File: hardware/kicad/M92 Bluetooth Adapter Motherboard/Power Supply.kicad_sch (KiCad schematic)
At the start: 35 parts, among them IC11 MCP1702T-5002E_CB, IC12 TPS22810DBVR, IC13 TPS22917DBVR, IC4 NJU7031D, IC4 TL7660IDR, J1 Conn_External_Power, J4 B2B-XH-A, J5 B2B-XH-A, J9 B6B-XH-A

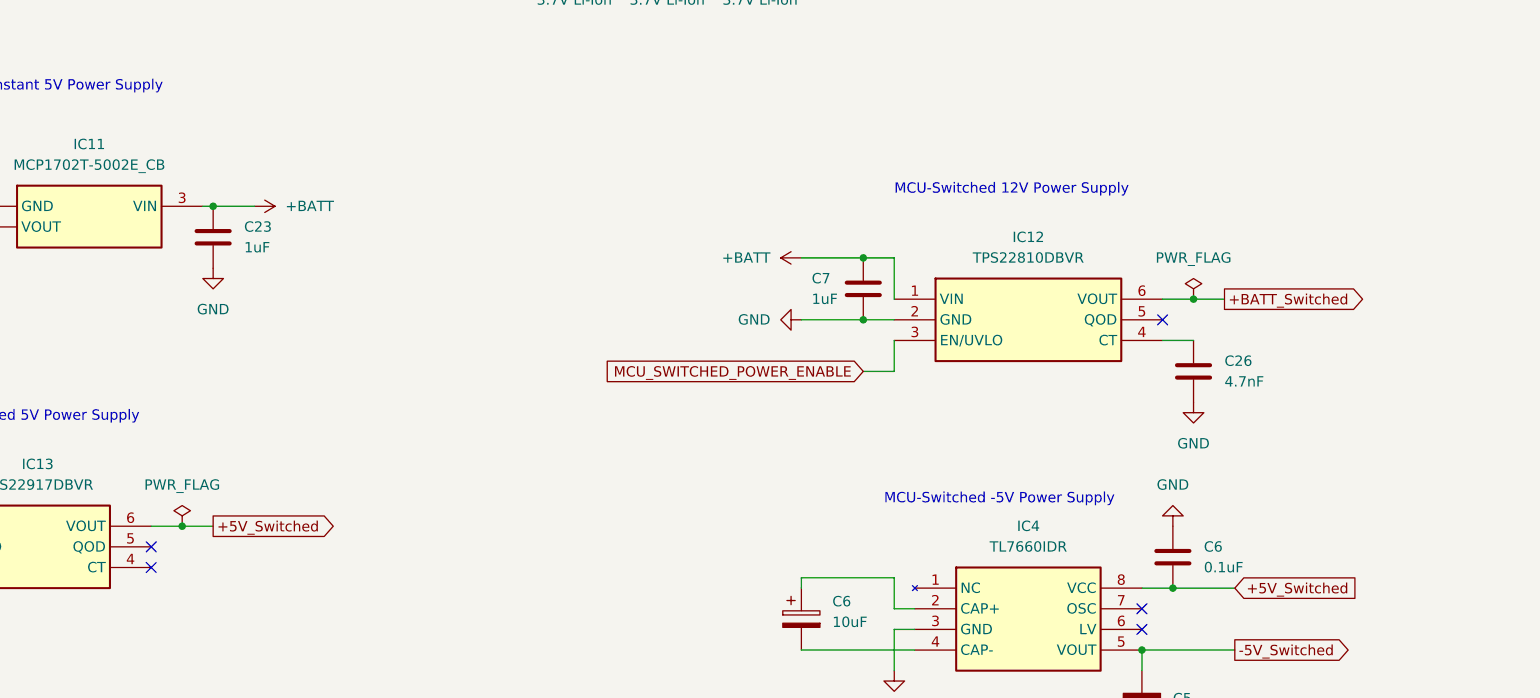
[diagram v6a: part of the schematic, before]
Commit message: Minor circuit and PCB layout adjustments
* Enable quick output discharge feature of both load switches.
* Change a decoupling cap from 1uF to 0.1uF for consistency.
* Fix incorrect labeling on the PCB of the BT module connector pinout.
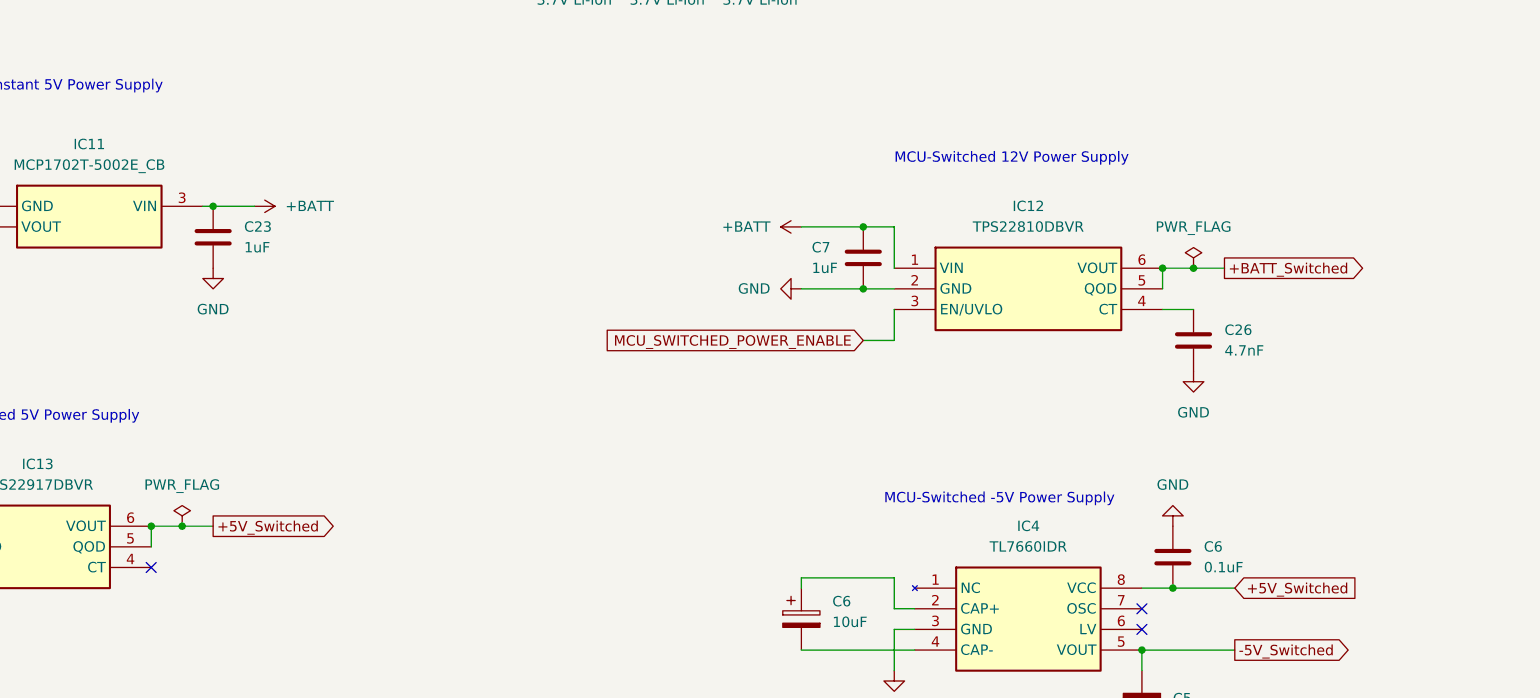
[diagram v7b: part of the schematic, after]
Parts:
- C27, C28: JLCPCB Part # C4747962 -> C2977467
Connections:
- net +5V_Switched: now also IC13.5 (QOD)
- net +BATT_Switched: now also IC12.5 (QOD)
- no-connect marks 8 -> 6
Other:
- moved on the sheet: C26, C7, IC12

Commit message: Minor schematic/pcb fixes
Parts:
- IC11: Mouser Price/Stock https://www.mouser.co.uk/ProductDetail/Microchip-Technology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 -> https://www.mouser.com/ProductDetail/Microchip-Technology/M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
- IC12, IC13: Mouser Price/Stock https://www.mouser.co.uk/ProductDetail/Texas-Instruments/TP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 -> https://www.mouser.com/ProductDetail/Texas-Instruments/TPS2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
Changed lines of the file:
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@@
       (effects (font (size 1.27 1.27)) (justify left top) hide)
     )
-    (property "Mouser Price/Stock" "https://www.mouser.co.uk/ProductDetail/Microchip-Technology/MCP1702T-5002E-CB?qs=jZi1jxfVU95NUMznXPYCsw%3D%3D" (at 95.25 687.63 0)
+    (property "Mouser Price/Stock" "https://www.mouser.com/ProductDetail/Microchip-Technology/MCP1702T-5002E-CB?qs=jZi1jxfVU95NUMznXPYCsw%3D%3D" (at 95.25 687.63 0)
       (effects (font (size 1.27 1.27)) (justify left top) hide)
     )
@@
       (effects (font (size 1.27 1.27)) (justify left top) hide)
     )
-    (property "Mouser Price/Stock" "https://www.mouser.co.uk/ProductDetail/Texas-Instruments/TPS22810DBVR?qs=34RfhUjJmKcFqeJVMZZhPA%3D%3D" (at 213.36 695.25 0)
+    (property "Mouser Price/Stock" "https://www.mouser.com/ProductDetail/Texas-Instruments/TPS22810DBVR?qs=34RfhUjJmKcFqeJVMZZhPA%3D%3D" (at 213.36 695.25 0)
       (effects (font (size 1.27 1.27)) (justify left top) hide)
     )
@@
       (effects (font (size 1.27 1.27)) (justify left top) hide)
     )
-    (property "Mouser Price/Stock" "https://www.mouser.co.uk/ProductDetail/Texas-Instruments/TPS22917DBVR?qs=r5DSvlrkXmI%2FDlZ5ksgkuQ%3D%3D" (at 88.9 727 0)
-      (effects (font (size 1.27 1.27)) (justify left top) hide)
-    )
+    (property "Mouser Price/Stock" "https://www.mouser.com/ProductDetail/Texas-Instruments/TPS22917DBVR?qs=r5DSvlrkXmI%2FDlZ5ksgkuQ%3D%3D" (at 88.9 727 0)
+      (effects (font (size 1.27 1.27)) (justify left top) hide)
+    )
